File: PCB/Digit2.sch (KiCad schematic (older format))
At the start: 1 part

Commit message: Worked on PCB.
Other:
- moved on the sheet: D3B
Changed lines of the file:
@@
 L LED_Array D3
 U 2 1 54BC7639
-P 4900 4100
-F 0 "D3" H 4900 5250 50  0000 C CNN
-F 1 "LED_Array" H 4900 5350 50  0000 C CNN
-F 2 "Custom:LED-ARRAY" H 4900 5025 50  0001 C CNN
-F 3 "" H 4900 5025 50  0000 C CNN
-	2    4900 4100
+P 3750 4150
+F 0 "D3" H 3750 5300 50  0000 C CNN
+F 1 "LED_Array" H 3750 5400 50  0000 C CNN
+F 2 "Custom:LED-ARRAY" H 3750 5075 50  0001 C CNN
+F 3 "" H 3750 5075 50  0000 C CNN
+	2    3750 4150
 	1    0    0    -1
 $EndComp

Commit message: Updated schematic.
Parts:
- added Q? (x14): FDG1024NZ, SC70-6, symbol FDG1024NZ
- added R? (x14): 10K, symbol R
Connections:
- net labels added: D1A1, D1A2, D1A3, D1A4, D1A5, D1A6, D1S1G, D1S1R, D1S2G, D1S2R, D1S3G, D1S3R, D1S4G, D1S4R, D1S5G, D1S5R, D1S6G, D1S6R, D1S7G, D1S7R, GND
- wire segments 0 -> 257
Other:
- moved on the sheet: D3B

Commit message: Updated schematic.
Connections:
- net labels added: D2A1, D2A2, D2A3, D2A4, D2A5, D2A6, D2S1G, D2S1R, D2S2G, D2S2R, D2S3G, D2S3R, D2S4G, D2S4R, D2S5G, D2S5R, D2S6G, D2S6R, D2S7G, D2S7R
- net labels removed: D1A1, D1A2, D1A3, D1A4, D1A5, D1A6, D1S1G, D1S1R, D1S2G, D1S2R, D1S3G, D1S3R, D1S4G, D1S4R, D1S5G, D1S5R, D1S6G, D1S6R, D1S7G, D1S7R
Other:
- moved on the sheet: D3B, R?

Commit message: Updated mosfets.
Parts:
- removed Q? (x14): FDG1024NZ, SC70-6, symbol FDG1024NZ
- added Q? (x14): DMN2041LSD-13, SO-8, symbol DMN2041LSD-13
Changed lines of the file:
@@
 D2A6
-$Comp
-L FDG1024NZ Q?
-U 1 1 54E99F19
-P 1350 2350
-F 0 "Q?" H 1350 2201 40  0000 R CNN
-F 1 "FDG1024NZ" H 1350 2500 40  0000 R CNN
-F 2 "SC70-6" H 1220 2452 29  0000 C CNN
-F 3 "" H 1350 2350 60  0000 C CNN
-	1    1350 2350
-	1    0    0    -1
-$EndComp
-$Comp
-L FDG1024NZ Q?
-U 1 1 54E99F20
-P 2350 2350
-F 0 "Q?" H 2350 2201 40  0000 R CNN
-F 1 "FDG1024NZ" H 2350 2500 40  0000 R CNN
-F 2 "SC70-6" H 2220 2452 29  0000 C CNN
-F 3 "" H 2350 2350 60  0000 C CNN
-	1    2350 2350
-	1    0    0    -1
-$EndComp
 $Comp
 L R R?
@@
 $EndComp
 $Comp
-L FDG1024NZ Q?
-U 1 1 54E99F41
-P 1350 5050
-F 0 "Q?" H 1350 4901 40  0000 R CNN
-F 1 "FDG1024NZ" H 1350 5200 40  0000 R CNN
-F 2 "SC70-6" H 1220 5152 29  0000 C CNN
-F 3 "" H 1350 5050 60  0000 C CNN
-	1    1350 5050
-	1    0    0    -1
-$EndComp
-$Comp
 L R R?
 U 1 1 54E99F48
@@
 D2S5G
 $Comp
-L FDG1024NZ Q?
-U 1 1 54E99F66
-P 2350 5050
-F 0 "Q?" H 2350 4901 40  0000 R CNN
-F 1 "FDG1024NZ" H 2350 5200 40  0000 R CNN
-F 2 "SC70-6" H 2220 5152 29  0000 C CNN
-F 3 "" H 2350 5050 60  0000 C CNN
-	1    2350 5050
-	1    0    0    -1
-$EndComp
-$Comp
-L FDG1024NZ Q?
-U 1 1 54E99F6D
-P 1350 6825
-F 0 "Q?" H 1350 6676 40  0000 R CNN
-F 1 "FDG1024NZ" H 1350 6975 40  0000 R CNN
-F 2 "SC70-6" H 1220 6927 29  0000 C CNN
-F 3 "" H 1350 6825 60  0000 C CNN
-	1    1350 6825
-	1    0    0    -1
-$EndComp
-$Comp
 L R R?
 U 1 1 54E99F74
@@
 Text HLabel 1900 6875 0    50   Input ~ 0
 D2S4G
-$Comp
-L FDG1024NZ Q?
-U 1 1 54E99F90
-P 2350 6825
-F 0 "Q?" H 2350 6676 40  0000 R CNN
-F 1 "FDG1024NZ" H 2350 6975 40  0000 R CNN
-F 2 "SC70-6" H 2220 6927 29  0000 C CNN
-F 3 "" H 2350 6825 60  0000 C CNN
-	1    2350 6825
-	1    0    0    -1
-$EndComp
 Wire Wire Line
 	3705 1150 3705 950
@@
 Wire Wire Line
 	2450 6625 2450 6500
-$Comp
-L FDG1024NZ Q?
-U 1 1 54E9A0B2
-P 7700 1125
-F 0 "Q?" H 7700 976 40  0000 R CNN
-F 1 "FDG1024NZ" H 7700 1275 40  0000 R CNN
-F 2 "SC70-6" H 7570 1227 29  0000 C CNN
-F 3 "" H 7700 1125 60  0000 C CNN
-	1    7700 1125
-	1    0    0    -1
-$EndComp
 $Comp
 L R R?
@@
 Text HLabel 8250 1175 0    50   Input ~ 0
 D2S1G
-$Comp
-L FDG1024NZ Q?
-U 1 1 54E9A0D5
-P 8700 1125
-F 0 "Q?" H 8700 976 40  0000 R CNN
-F 1 "FDG1024NZ" H 8700 1275 40  0000 R CNN
-F 2 "SC70-6" H 8570 1227 29  0000 C CNN
-F 3 "" H 8700 1125 60  0000 C CNN
-	1    8700 1125
-	1    0    0    -1
-$EndComp
 Wire Wire Line
 	8250 1175 8500 1175
@@
 Wire Wire Line
 	8800 675  8800 925
-$Comp
-L FDG1024NZ Q?
-U 1 1 54E9A0EB
-P 7700 2625
-F 0 "Q?" H 7700 2476 40  0000 R CNN
-F 1 "FDG1024NZ" H 7700 2775 40  0000 R CNN
-F 2 "SC70-6" H 7570 2727 29  0000 C CNN
-F 3 "" H 7700 2625 60  0000 C CNN
-	1    7700 2625
-	1    0    0    -1
-$EndComp
 $Comp
 L R R?
@@
 Text HLabel 8250 2675 0    50   Input ~ 0
 D2S2G
-$Comp
-L FDG1024NZ Q?
-U 1 1 54E9A10E
-P 8700 2625
-F 0 "Q?" H 8700 2476 40  0000 R CNN
-F 1 "FDG1024NZ" H 8700 2775 40  0000 R CNN
-F 2 "SC70-6" H 8570 2727 29  0000 C CNN
-F 3 "" H 8700 2625 60  0000 C CNN
-	1    8700 2625
-	1    0    0    -1
-$EndComp
 Wire Wire Line
 	8250 2675 8500 2675
@@
 Wire Wire Line
 	8800 2125 8800 2425
-$Comp
-L FDG1024NZ Q?
-U 1 1 54E9A125
-P 7700 5485
-F 0 "Q?" H 7700 5336 40  0000 R CNN
-F 1 "FDG1024NZ" H 7700 5635 40  0000 R CNN
-F 2 "SC70-6" H 7570 5587 29  0000 C CNN
-F 3 "" H 7700 5485 60  0000 C CNN
-	1    7700 5485
-	1    0    0    -1
-$EndComp
 $Comp
 L R R?
@@
 Text HLabel 8250 5535 0    50   Input ~ 0
 D2S3G
-$Comp
-L FDG1024NZ Q?
-U 1 1 54E9A148
-P 8700 5485
-F 0 "Q?" H 8700 5336 40  0000 R CNN
-F 1 "FDG1024NZ" H 8700 5635 40  0000 R CNN
-F 2 "SC70-6" H 8570 5587 29  0000 C CNN
-F 3 "" H 8700 5485 60  0000 C CNN
-	1    8700 5485
-	1    0    0    -1
-$EndComp
 Wire Wire Line
 	8250 5535 8500 5535
@@
 Wire Wire Line
 	7800 750  7800 925
-$Comp
-L FDG1024NZ Q?
-U 1 1 54E9A160
-P 7700 4010
-F 0 "Q?" H 7700 3861 40  0000 R CNN
-F 1 "FDG1024NZ" H 7700 4160 40  0000 R CNN
-F 2 "SC70-6" H 7570 4112 29  0000 C CNN
-F 3 "" H 7700 4010 60  0000 C CNN
-	1    7700 4010
-	1    0    0    -1
-$EndComp
 $Comp
 L R R?
@@
 Text HLabel 8250 4060 0    50   Input ~ 0
 D2S7G
-$Comp
-L FDG1024NZ Q?
-U 1 1 54E9A183
-P 8700 4010
-F 0 "Q?" H 8700 3861 40  0000 R CNN
-F 1 "FDG1024NZ" H 8700 4160 40  0000 R CNN
-F 2 "SC70-6" H 8570 4112 29  0000 C CNN
-F 3 "" H 8700 4010 60  0000 C CNN
-	1    8700 4010
-	1    0    0    -1
-$EndComp
 Wire Wire Line
 	8250 4060 8500 4060
@@
 EndData
 $EndBitmap
+$Comp
+L DMN2041LSD-13 Q?
+U 1 1 54ED9369
+P 1350 2350
+F 0 "Q?" H 1350 2201 40  0000 R CNN
+F 1 "DMN2041LSD-13" H 1350 2500 40  0000 R CNN
+F 2 "SO-8" H 1220 2452 29  0001 C CNN
+F 3 "" H 1350 2350 60  0000 C CNN
+	1    1350 2350
+	1    0    0    -1
+$EndComp
+$Comp
+L DMN2041LSD-13 Q?
+U 2 1 54ED93D8
+P 2350 2350
+F 0 "Q?" H 2350 2201 40  0000 R CNN
+F 1 "DMN2041LSD-13" H 2350 2500 40  0000 R CNN
+F 2 "SO-8" H 2220 2452 29  0001 C CNN
+F 3 "" H 2350 2350 60  0000 C CNN
+	2    2350 2350
+	1    0    0    -1
+$EndComp
+$Comp
+L DMN2041LSD-13 Q?
+U 1 1 54ED97BE
+P 1350 5050
+F 0 "Q?" H 1350 4901 40  0000 R CNN
+F 1 "DMN2041LSD-13" H 1350 5200 40  0000 R CNN
+F 2 "SO-8" H 1220 5152 29  0001 C CNN
+F 3 "" H 1350 5050 60  0000 C CNN
+	1    1350 5050
+	1    0    0    -1
+$EndComp
+$Comp
+L DMN2041LSD-13 Q?
+U 2 1 54ED9809
+P 2350 5050
+F 0 "Q?" H 2350 4901 40  0000 R CNN
+F 1 "DMN2041LSD-13" H 2350 5200 40  0000 R CNN
+F 2 "SO-8" H 2220 5152 29  0001 C CNN
+F 3 "" H 2350 5050 60  0000 C CNN
+	2    2350 5050
+	1    0    0    -1
+$EndComp
+$Comp
+L DMN2041LSD-13 Q?
+U 1 1 54ED9B65
+P 1350 6825
+F 0 "Q?" H 1350 6676 40  0000 R CNN
+F 1 "DMN2041LSD-13" H 1350 6975 40  0000 R CNN
+F 2 "SO-8" H 1220 6927 29  0001 C CNN
+F 3 "" H 1350 6825 60  0000 C CNN
+	1    1350 6825
+	1    0    0    -1
+$EndComp
+$Comp
+L DMN2041LSD-13 Q?
+U 2 1 54ED9BC8
+P 2350 6825
+F 0 "Q?" H 2350 6676 40  0000 R CNN
+F 1 "DMN2041LSD-13" H 2350 6975 40  0000 R CNN
+F 2 "SO-8" H 2220 6927 29  0001 C CNN
+F 3 "" H 2350 6825 60  0000 C CNN
+	2    2350 6825
+	1    0    0    -1
+$EndComp
+$Comp
+L DMN2041LSD-13 Q?
+U 1 1 54EDA4B3
+P 7700 5485
+F 0 "Q?" H 7700 5336 40  0000 R CNN
+F 1 "DMN2041LSD-13" H 7700 5635 40  0000 R CNN
+F 2 "SO-8" H 7570 5587 29  0001 C CNN
+F 3 "" H 7700 5485 60  0000 C CNN
+	1    7700 5485
+	1    0    0    -1
+$EndComp
+$Comp
+L DMN2041LSD-13 Q?
+U 2 1 54EDA516
+P 8700 5485
+F 0 "Q?" H 8700 5336 40  0000 R CNN
+F 1 "DMN2041LSD-13" H 8700 5635 40  0000 R CNN
+F 2 "SO-8" H 8570 5587 29  0001 C CNN
+F 3 "" H 8700 5485 60  0000 C CNN
+	2    8700 5485
+	1    0    0    -1
+$EndComp
+$Comp
+L DMN2041LSD-13 Q?
+U 1 1 54EDAAA7
+P 7700 4010
+F 0 "Q?" H 7700 3861 40  0000 R CNN
+F 1 "DMN2041LSD-13" H 7700 4160 40  0000 R CNN
+F 2 "SO-8" H 7570 4112 29  0001 C CNN
+F 3 "" H 7700 4010 60  0000 C CNN
+	1    7700 4010
+	1    0    0    -1
+$EndComp
+$Comp
+L DMN2041LSD-13 Q?
+U 2 1 54EDAB10
+P 8700 4010
+F 0 "Q?" H 8700 3861 40  0000 R CNN
+F 1 "DMN2041LSD-13" H 8700 4160 40  0000 R CNN
+F 2 "SO-8" H 8570 4112 29  0001 C CNN
+F 3 "" H 8700 4010 60  0000 C CNN
+	2    8700 4010
+	1    0    0    -1
+$EndComp
+$Comp
+L DMN2041LSD-13 Q?
+U 1 1 54EDB371
+P 7700 2625
+F 0 "Q?" H 7700 2476 40  0000 R CNN
+F 1 "DMN2041LSD-13" H 7700 2775 40  0000 R CNN
+F 2 "SO-8" H 7570 2727 29  0001 C CNN
+F 3 "" H 7700 2625 60  0000 C CNN
+	1    7700 2625
+	1    0    0    -1
+$EndComp
+$Comp
+L DMN2041LSD-13 Q?
+U 2 1 54EDB3DA
+P 8700 2625
+F 0 "Q?" H 8700 2476 40  0000 R CNN
+F 1 "DMN2041LSD-13" H 8700 2775 40  0000 R CNN
+F 2 "SO-8" H 8570 2727 29  0001 C CNN
+F 3 "" H 8700 2625 60  0000 C CNN
+	2    8700 2625
+	1    0    0    -1
+$EndComp
+$Comp
+L DMN2041LSD-13 Q?
+U 1 1 54EDB656
+P 7700 1125
+F 0 "Q?" H 7700 976 40  0000 R CNN
+F 1 "DMN2041LSD-13" H 7700 1275 40  0000 R CNN
+F 2 "SO-8" H 7570 1227 29  0001 C CNN
+F 3 "" H 7700 1125 60  0000 C CNN
+	1    7700 1125
+	1    0    0    -1
+$EndComp
+$Comp
+L DMN2041LSD-13 Q?
+U 2 1 54EDB6BF
+P 8700 1125
+F 0 "Q?" H 8700 976 40  0000 R CNN
+F 1 "DMN2041LSD-13" H 8700 1275 40  0000 R CNN
+F 2 "SO-8" H 8570 1227 29  0001 C CNN
+F 3 "" H 8700 1125 60  0000 C CNN
+	2    8700 1125
+	1    0    0    -1
+$EndComp
 $EndSCHEMATC

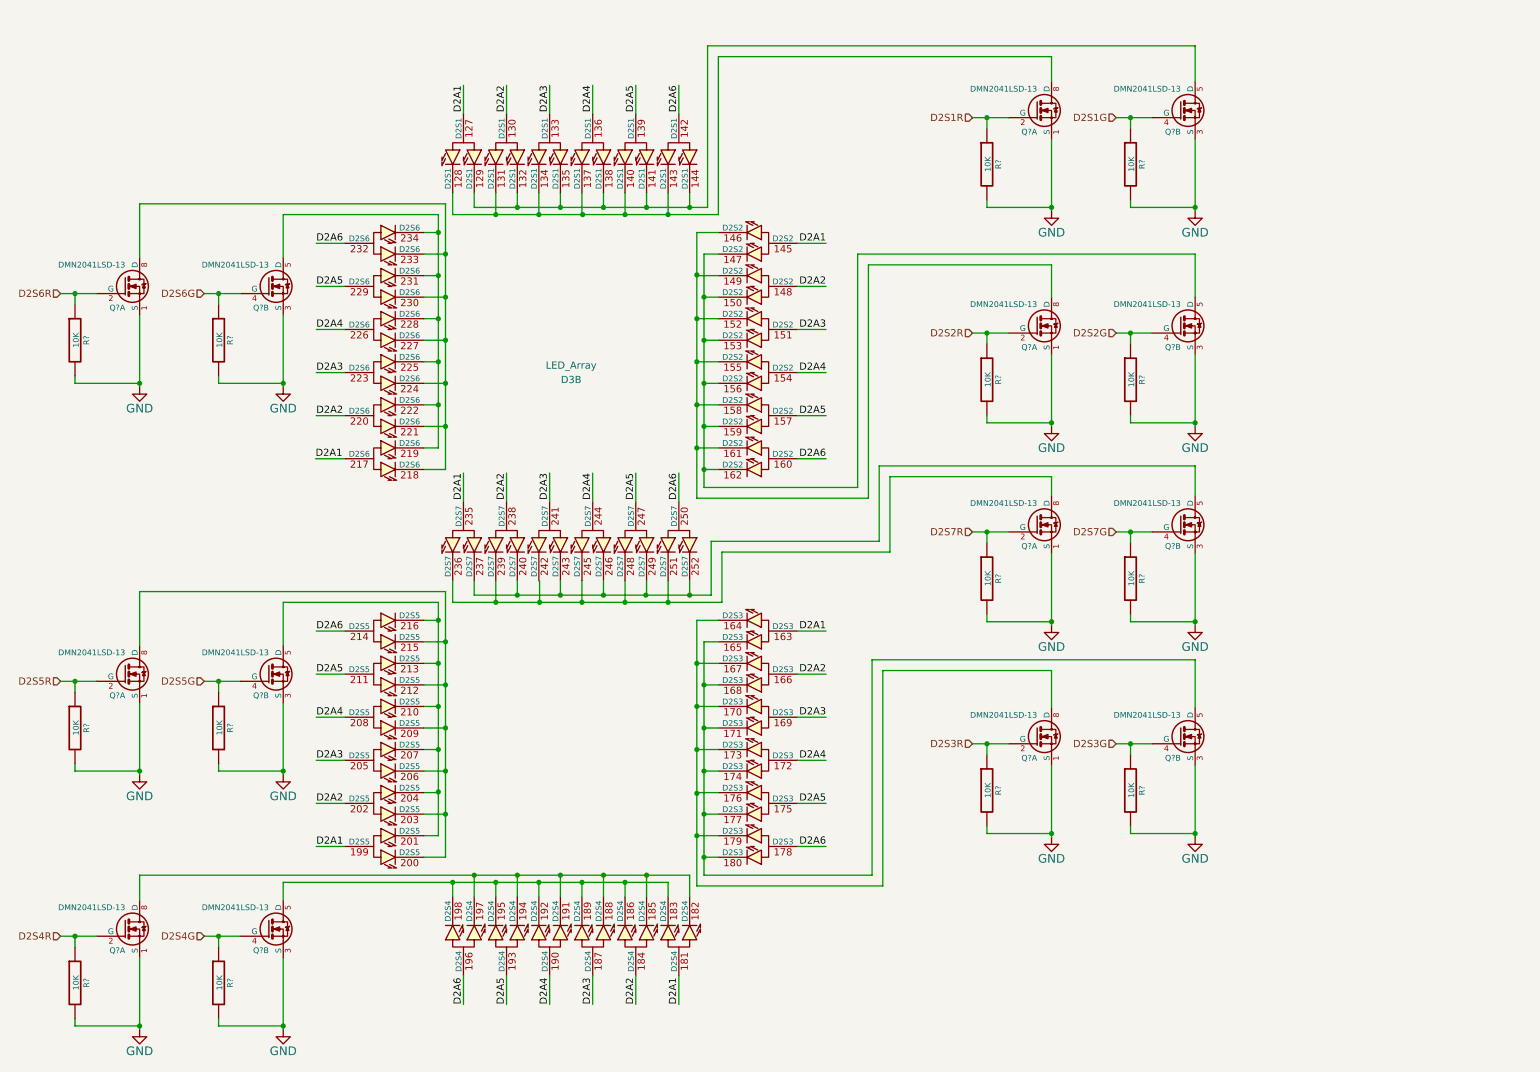
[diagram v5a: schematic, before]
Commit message: Added additional mosfets.
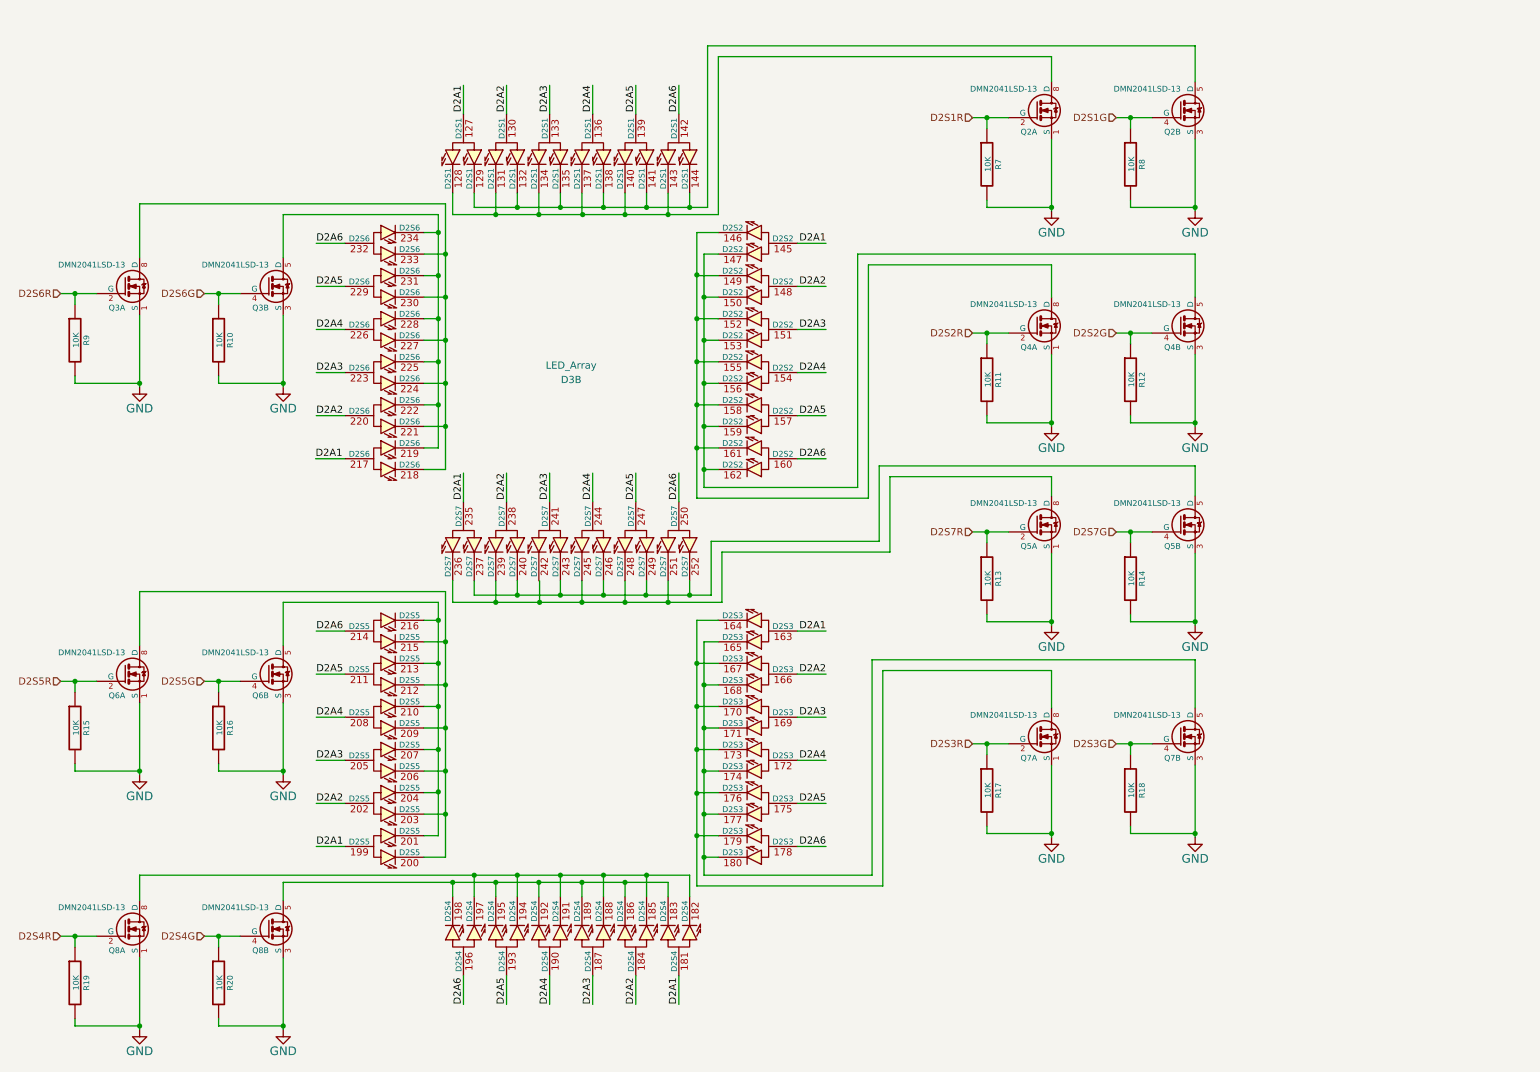
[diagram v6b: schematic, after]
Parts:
- Q2, Q3, Q4, Q5, Q6, Q7, Q8: renamed from Q?; footprint SO-8 -> Power_Integrations:SO-8
- R10, R11, R12, R13, R14, R15, R16, R17, R18, R19, R20, R7, R8, R9: renamed from R?; footprint (none) -> Resistors_SMD:R_0603_HandSoldering

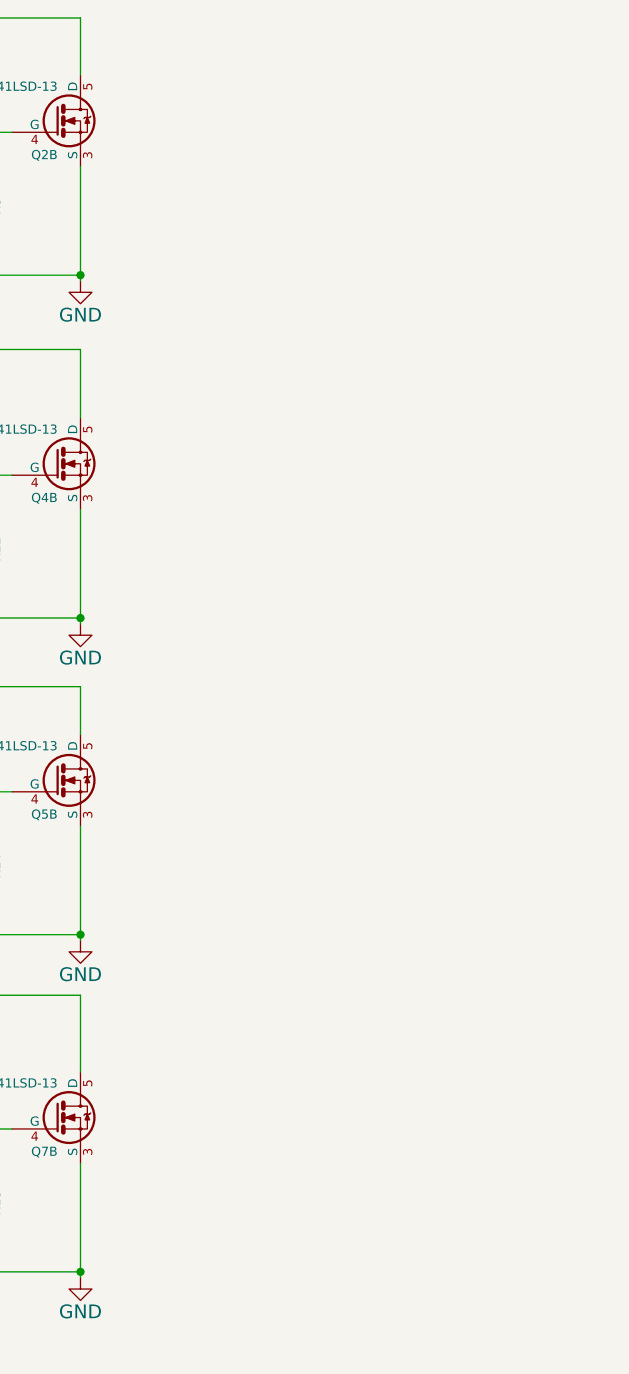
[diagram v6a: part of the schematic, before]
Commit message: Added additional mosfets.
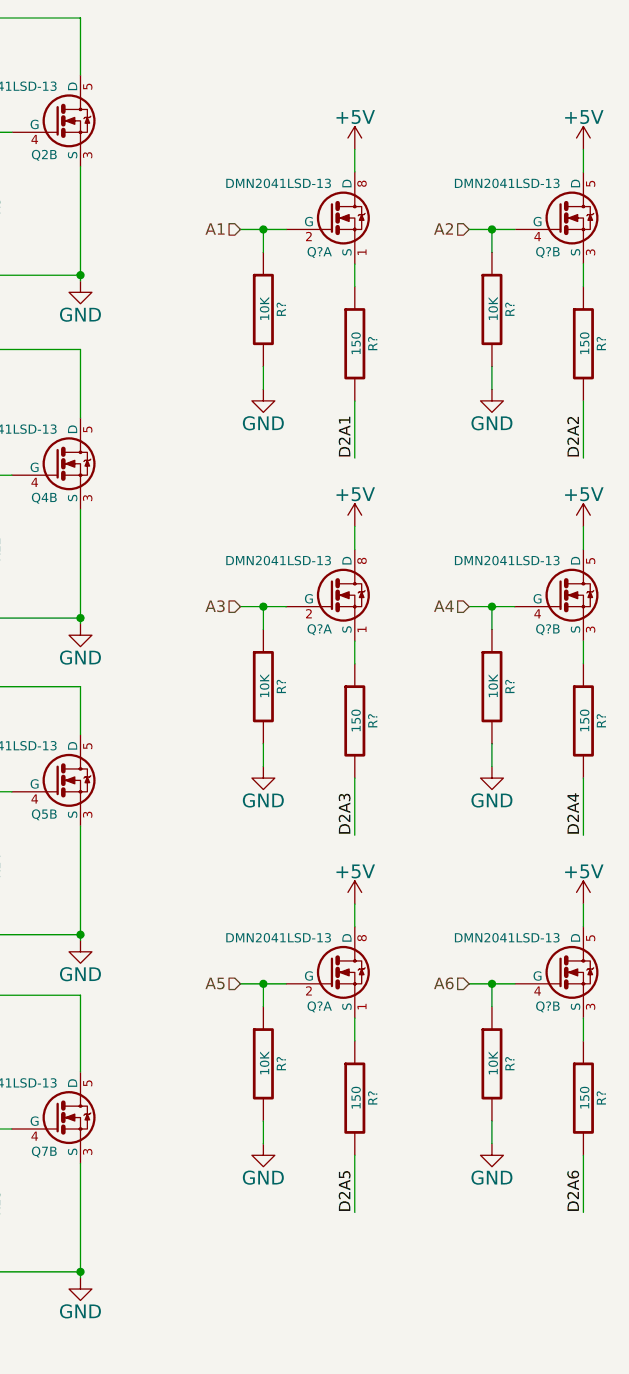
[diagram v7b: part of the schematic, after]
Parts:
- added Q? (x6): DMN2041LSD-13, SO-8, symbol DMN2041LSD-13
- added R? (x6): 10K, Resistors_SMD:R_0603_HandSoldering, symbol R
- added R? (x6): 150, Resistors_SMD:R_0603_HandSoldering, symbol R
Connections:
- net D2A1: now also R?.2
- net D2A2: now also R?.2
- net D2A3: now also R?.2
- net D2A4: now also R?.2
- net D2A5: now also R?.2
- net D2A6: now also R?.2
- net GND: now also R?.2, R?.2, R?.2, R?.2, R?.2, R?.2
- new net: Q?.1 (S), R?.1 (x3)
- new net: Q?.3 (S), R?.1 (x3)
- new net +5V: Q?.5 (D), Q?.5 (D), Q?.5 (D), Q?.8 (D), Q?.8 (D), Q?.8 (D)
- new net A1: Q?.2 (G), R?.1
- new net A2: Q?.4 (G), R?.1
- new net A3: Q?.2 (G), R?.1
- new net A4: Q?.4 (G), R?.1
- new net A5: Q?.2 (G), R?.1
- new net A6: Q?.4 (G), R?.1

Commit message: Edit PCB.
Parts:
- gave numbers to parts that had none: 15
